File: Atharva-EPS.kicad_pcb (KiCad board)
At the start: 2 copper layers, 86.3 x 96.9 mm, 98 parts, among them J101 Conn_01x02_Female, J102 Conn_01x02_Female, J103 Conn_01x02_Female, J104 Conn_01x02_Female, J105 Conn_02x26_Odd_Even, J106 Conn_02x26_Odd_Even, J107 Conn_01x05_Female, J108 Conn_01x05_Female, J109 Conn_01x05_Female, J110 Conn_01x05_Female, J111 Conn_01x05_Female, J112 Conn_01x05_Female, Q101 P-MOSFET-SOT23-3, Q102 2N3906, Q103 2N3906, Q104 IRLML2060, Q105 IRLML2060, Q106 IRLML2060, Q107 IRLML2060, U101 LT1930ES5TRMPBF, U102 LT1930ES5TRMPBF, U103 S-8209AXXT, U104 S-8209AXXT, U107 LT3652EMSE

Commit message: EPS version 1,0
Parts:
- removed G***: LOGO, time:timeFP
- removed G***: LOGO, drake1:drake1FP
- removed G***: LOGO, drake1:drake2FP
- removed G***: LOGO, Sunny:SunnyFP
- removed Q101: P-MOSFET-SOT23-3, TSM2307CX:SOT23-3
- removed R122: 280, Resistor_SMD:R_0805_2012Metric
- removed REF**: OSHW-Logo2_7.3x6mm_SilkScreen, Symbol:OSHW-Logo2_7.3x6mm_SilkScreen
- added C108: Test, Capacitor_SMD:C_0805_2012Metric, F.Cu at (102.0, 70.2)
- added C109: Test, Capacitor_SMD:C_0805_2012Metric, F.Cu at (93.3, 103.0)
- added C111: Test, Capacitor_SMD:C_0805_2012Metric, F.Cu at (102.2, 81.1)
- added C112: Test, Capacitor_SMD:C_0805_2012Metric, F.Cu at (97.3, 101.4)
- added C114: Test, Capacitor_SMD:C_0805_2012Metric, F.Cu at (102.0, 73.5)
- added C115: Test, Capacitor_SMD:C_0805_2012Metric, F.Cu at (101.4, 100.4)
- added C117: Test, Capacitor_SMD:C_0805_2012Metric, F.Cu at (102.0, 77.3)
- added C118: Test, Capacitor_SMD:C_0805_2012Metric, F.Cu at (105.7, 98.9)
- added D103: D_Schottky, Diode_SMD:D_0805_2012Metric, F.Cu at (100.0, 65.2)
- added D104: D_Schottky, Diode_SMD:D_0805_2012Metric, F.Cu at (97.6, 85.4)
- added D106: D_Schottky, Diode_SMD:D_0805_2012Metric, F.Cu at (96.9, 112.7)
- added D107: D_Schottky, Diode_SMD:D_0805_2012Metric, F.Cu at (132.8, 139.8)
- added D108: D_Schottky, Diode_SMD:D_0805_2012Metric, F.Cu at (136.5, 142.8)
- added D109: D_Schottky, Diode_SMD:D_0805_2012Metric, F.Cu at (107.7, 69.7)
- C101, C102: value C -> 0.1uF
- C103, C104: value C -> 4.7uF; footprint Capacitor_SMD:C_0805_2012Metric -> Capacitor_SMD:C_1206_3216Metric
- D101: value 1N5817 -> D_Schottky; footprint Diode_THT:D_DO-41_SOD81_P10.16mm_Horizontal -> Diode_SMD:D_0805_2012Metric
- D105: footprint Diode_SMD:D_1210_3225Metric -> Diode_SMD:D_0805_2012Metric
- H101, H102, H103, H104: value MountingHole -> MountingHole_Pad
- L101, L102: value L -> 10uH
- moved D105 36.8 mm to (103.1, 89.9)
- moved R132 29.1 mm to (121.7, 103.5), turned to 90 degrees
- moved R129 25.4 mm to (113.6, 106.5)
- moved D101 24.9 mm to (109.8, 93.7), turned to 90 degrees
- moved C104 20.4 mm to (109.8, 98.9), turned to 90 degrees
- moved U102 19.2 mm to (115.9, 98.1)
- moved R130 18.6 mm to (115.5, 102.7)
- moved C101 17.0 mm to (117.9, 94.8)
- moved L102 16.4 mm to (112.8, 93.2), turned to -90 degrees
- moved R123 15.0 mm to (127.1, 73.5), turned to 90 degrees
- moved L101 11.9 mm to (112.6, 66.3), turned to 90 degrees
- moved R125 9.65 mm to (122.6, 67.7)
- moved C103 9.61 mm to (109.5, 73.3), turned to 90 degrees
- moved C102 7.57 mm to (117.2, 67.7)
- moved R126 6.71 mm to (112.1, 80.3), turned to 90 degrees
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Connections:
- net Net-(BT101-Pad2) renamed /-Batt_1
- net Net-(Q102-Pad1) renamed /+Batt_1
- net Net-(R111-Pad1) renamed /+Batt_2
- BT101 pad 1: Net-(R115-Pad1) -> Net-(BT101-Pad1)
- BT102 pad 2: Net-(BT104-Pad1) -> Net-(J101-Pad1)
- BT104 pad 2: Net-(BT104-Pad1) -> Net-(J101-Pad1)
- C104 pad 2: +5V -> +3V3
- C107 pad 2: B -> /-Batt_2
- C110 pad 1: +BATT -> Solar_Out
- C110 pad 2: +BATT -> GND
- C116 pad 1: +BATT -> Batt_in
- C116 pad 2: +BATT -> GND
- D101 pad 1: Net-(D101-Pad1) -> +3V3
- D101 pad 2: +5V -> Net-(L102-Pad1)
- D102 pad 2: +BATT -> Solar_Out
- D105 pad 1: +BATT -> Solar_Out
- D105 pad 2: Net-(BT104-Pad1) -> /Solar_3
- D110 pad 2: +BATT -> GND
- D111 pad 2: +BATT -> Batt_in
- D114 pad 2: +BATT -> Batt_in
- H101 pad 1: (no net) -> GND
- H102 pad 1: (no net) -> GND
- H103 pad 1: (no net) -> GND
- H104 pad 1: (no net) -> GND
- J101 pad 1: Net-(BT104-Pad1) -> Net-(J101-Pad1)
- J101 pad 2: Net-(BT104-Pad1) -> /-Batt_2
- J102 pad 1: Net-(BT104-Pad1) -> Net-(J102-Pad1)
- J103 pad 2: Net-(J103-Pad2) -> Net-(BT101-Pad1)
- J104 pad 1: Net-(J103-Pad2) -> Net-(R115-Pad1)
- J104 pad 2: Net-(D101-Pad1) -> Net-(J102-Pad1)
- J105 pad 27: +5V -> +3V3
- J105 pad 28: +5V -> +3V3
- J105 pad 29: +5V -> GND
- J105 pad 32: +BATT -> GND
- J105 pad 44: +BATT -> unconnected-(J105-Pad44)
- J106 pad 22: +5V -> unconnected-(J106-Pad22)
- J106 pad 23: +5V -> unconnected-(J106-Pad23)
- J106 pad 24: +5V -> unconnected-(J106-Pad24)
- J106 pad 25: +5V -> unconnected-(J106-Pad25)
- J106 pad 30: +BATT -> unconnected-(J106-Pad30)
- J106 pad 31: +BATT -> unconnected-(J106-Pad31)
- J106 pad 32: +BATT -> Batt_in
- J106 pad 33: +BATT -> unconnected-(J106-Pad33)
- J106 pad 34: +BATT -> unconnected-(J106-Pad34)
- J106 pad 35: +BATT -> unconnected-(J106-Pad35)
- J106 pad 36: +BATT -> unconnected-(J106-Pad36)
- J106 pad 37: +BATT -> unconnected-(J106-Pad37)
- J106 pad 38: +BATT -> unconnected-(J106-Pad38)
- J106 pad 39: +BATT -> unconnected-(J106-Pad39)
- J106 pad 40: +BATT -> unconnected-(J106-Pad40)
- J106 pad 41: +BATT -> I2C_DATA
- J106 pad 42: +BATT -> unconnected-(J106-Pad42)
- J106 pad 43: +BATT -> I2C_CLK
- J107 pad 1: Net-(BT104-Pad1) -> /Solar_1
- J107 pad 2: Net-(BT104-Pad1) -> GND
- J108 pad 1: Net-(BT104-Pad1) -> /Solar_2
- J108 pad 2: Net-(BT104-Pad1) -> GND
- J109 pad 1: Net-(BT104-Pad1) -> /Solar_3
- J109 pad 2: Net-(BT104-Pad1) -> GND
- J110 pad 1: Net-(BT104-Pad1) -> /Solar_4
- J110 pad 2: Net-(BT104-Pad1) -> GND
- J111 pad 1: Net-(BT104-Pad1) -> /Solar_5
- J112 pad 1: Net-(BT104-Pad1) -> /Solar_6
- L101 pad 1: +5V -> Net-(L101-Pad1)
- L102 pad 1: +5V -> Net-(L102-Pad1)
- Q105 pad 2: B -> /-Batt_2
- Q107 pad 2: B -> /-Batt_2
- R106 pad 2: B -> /-Batt_2
- R108 pad 2: B -> /-Batt_2
- R114 pad 2: +BATT -> Batt_in
- R117 pad 1: Net-(C110-Pad1) -> Solar_Out
- R119 pad 2: Net-(R115-Pad1) -> Net-(BT101-Pad1)
- R121 pad 2: +BATT -> Batt_in
- R127 pad 2: +BATT -> Batt_in
- R144 pad 2: B -> /-Batt_2
- TP102 pad 1: +5V -> +3V3
- TP105 pad 1: +BATT -> Batt_in
- U102 pad 1: +5V -> +3V3
- U104 pad 5: B -> /-Batt_2
- U104 pad 6: Net-(R107-Pad2) -> Net-(R105-Pad2)
- U104 pad 7: Net-(R105-Pad2) -> Net-(R107-Pad2)
- U107 pad 1: Net-(C110-Pad1) -> Solar_Out
- U107 pad 13: +BATT -> GND
- U107 pad 3: Net-(C110-Pad1) -> Solar_Out
- U107 pad 9: +BATT -> Batt_in
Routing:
- net Net-(BT104-Pad1): track 468.2 -> 85.3 mm, vias 4 -> 2
- net Solar_Out: track 0.00 -> 193.4 mm, vias 0 -> 2
- net Net-(BT101-Pad1): track 0.00 -> 124.5 mm, vias 0 -> 1
- net +3V3: track 0.00 -> 117.5 mm
- net +BATT: track 182.1 -> 66.2 mm, vias 8 -> 1
- net Net-(J101-Pad1): track 0.00 -> 115.4 mm, vias 0 -> 3
- net B: track 114.0 -> 0.00 mm, vias 3 -> 0
- net /-Batt_2: track 0.00 -> 106.7 mm, vias 0 -> 1
- net Net-(R115-Pad1): track 109.9 -> 14.4 mm, vias 3 -> 0
- net Net-(D101-Pad1): track 86.9 -> 0.00 mm
- net Batt_in: track 0.00 -> 85.7 mm, vias 0 -> 2
- net +5V: track 137.7 -> 93.2 mm, vias 4 -> 1
- net Net-(J102-Pad1): track 0.00 -> 30.3 mm
- net Net-(Q103-Pad3): track 29.3 -> 54.7 mm, vias 2 -> 0
- net Net-(R132-Pad2): track 26.1 -> 6.13 mm, vias 2 -> 0
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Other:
- board text added: "+"
- board text added: "{dblquote}caps, diodes and hope{dblquote}"
- board text removed: "Yeah, I've got time."

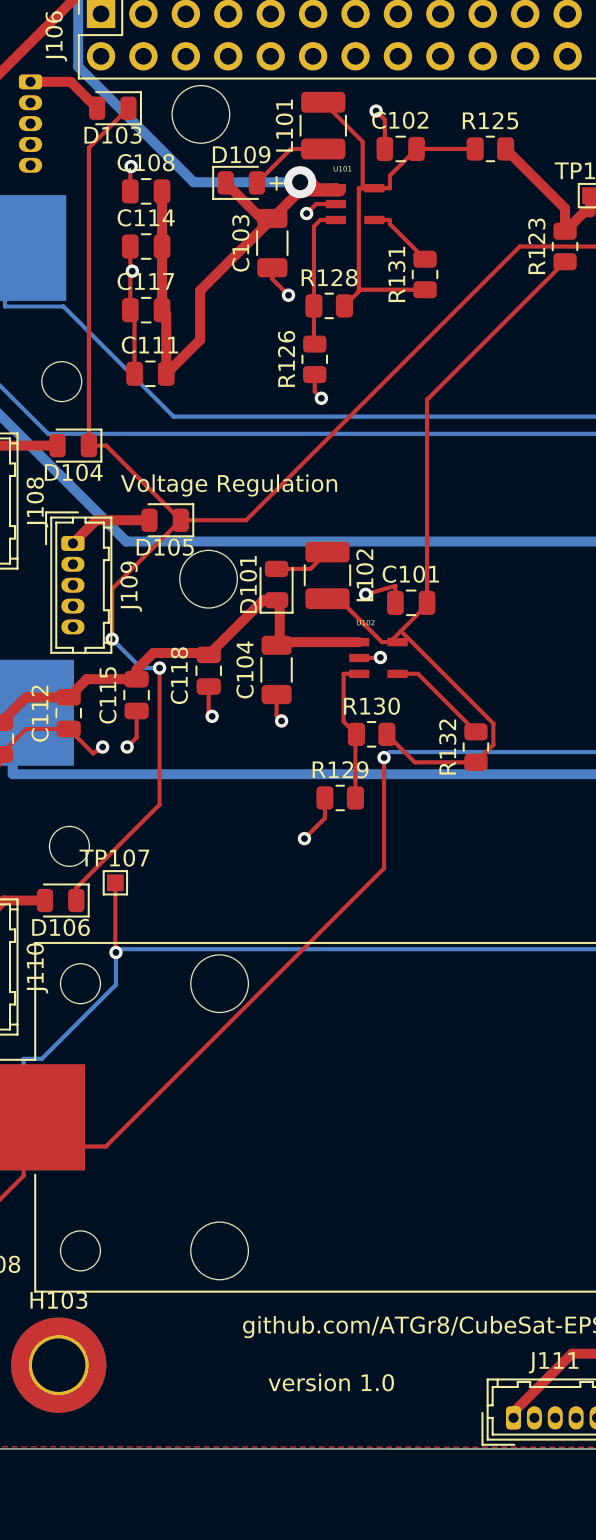
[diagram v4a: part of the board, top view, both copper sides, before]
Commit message: EPS version 1.0 - fixed minor error of having placed the reistors at the wrong spot in the buck boost
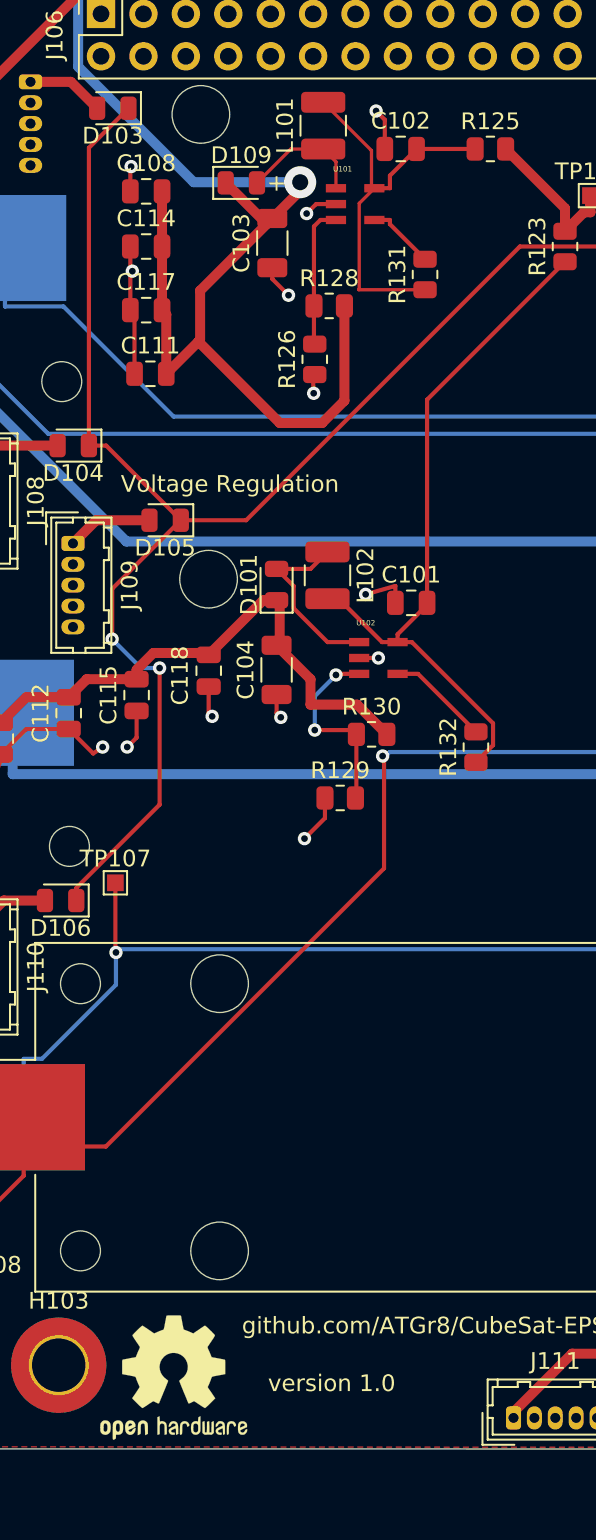
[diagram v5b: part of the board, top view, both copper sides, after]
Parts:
- added REF**: OSHW-Logo2_9.8x8mm_SilkScreen, Symbol:OSHW-Logo2_9.8x8mm_SilkScreen, F.Cu at (103.6, 141.2)
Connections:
- D101 pad 2: Net-(L102-Pad1) -> Net-(D101-Pad2)
- D109 pad 2: Net-(L101-Pad1) -> Net-(D109-Pad2)
- L101 pad 1: Net-(L101-Pad1) -> Net-(D109-Pad2)
- L102 pad 1: Net-(L102-Pad1) -> Net-(D101-Pad2)
- R128 pad 2: Net-(C102-Pad2) -> +5V
- R130 pad 2: Net-(C101-Pad2) -> +3V3
- U101 pad 1: +5V -> Net-(D109-Pad2)
- U102 pad 1: +3V3 -> Net-(D101-Pad2)
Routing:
- net +5V: track 93.2 -> 106.8 mm
- net Net-(D101-Pad2): track 0.00 -> 11.0 mm
- net Net-(D109-Pad2): track 0.00 -> 7.97 mm
- net Net-(C101-Pad2): track 49.0 -> 42.7 mm
- net Net-(L101-Pad1): track 4.81 -> 0.00 mm
- net +3V3: track 117.5 -> 122.2 mm
- net Net-(L102-Pad1): track 3.47 -> 0.00 mm
- net Net-(U102-Pad3): track 8.70 -> 11.7 mm, vias 0 -> 2
- net Net-(C102-Pad2): track 25.9 -> 24.8 mm
- net GND: track 58.7 -> 57.9 mm
